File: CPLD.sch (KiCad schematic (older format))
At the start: 44 parts, among them J5 JTAG, J6 PMOD, Q1 IRLML6402, Q2 IRLML6402, SW2 SW_DIP_x06, U3 EPM7064STC100, X1 CFPS-72 50mhz

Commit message: started routing
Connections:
- wire segments 238 -> 236
- no-connect marks 8 -> 9
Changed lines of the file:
@@
 JTAG
-$Comp
-L THS-80:Altera-JTAG-10 J?
-U 1 1 5DC12FA5
-P 1000 1950
-AR Path="/5D0F9837/5DC12FA5" Ref="J?"  Part="1"
-AR Path="/5CFABACD/5D0BF766/5DC12FA5" Ref="J?"  Part="1"
-AR Path="/5D1AF052/5DC12FA5" Ref="J?"  Part="1"
-AR Path="/5DC12FA5" Ref="J?"  Part="1"
-AR Path="/5D70CA34/5DC12FA5" Ref="J5"  Part="1"
-F 0 "J5" H 1040 1950 50  0000 R CNN
-F 1 "JTAG" H 760 2450 50  0000 R CNN
-F 2 "Connector_PinHeader_2.54mm:PinHeader_2x05_P2.54mm_Vertical" V 850 2100 50  0001 C CNN
-F 3 "~" H -275 1400 50  0001 C CNN
-	1    1000 1950
-	1    0    0    -1
-$EndComp
 $Comp
 L power:VCC #PWR?
@@
 Wire Wire Line
 	900  1300 1200 1300
-Wire Wire Line
-	1500 1300 1500 1650
-Connection ~ 1200 1300
-Wire Wire Line
-	1200 1300 1500 1300
 Wire Wire Line
 	1500 1850 1700 1850
@@
 Text HLabel 7350 2075 2    50   Input ~ 0
 A[0..7]
-Text HLabel 3750 2400 0    50   Output ~ 0
-A[16..18]
 Text HLabel 7350 3150 2    50   Input ~ 0
 D[0..7]
@@
 L Device:R_Pack08 RN2
 U 1 1 5D75CC44
-P 10300 3300
-F 0 "RN2" V 9683 3300 50  0000 C CNN
-F 1 "680R" V 9774 3300 50  0000 C CNN
-F 2 "Resistor_SMD:R_Cat16-8" V 10775 3300 50  0001 C CNN
-F 3 "~" H 10300 3300 50  0001 C CNN
-	1    10300 3300
-	0    1    -1   0
-$EndComp
-Wire Wire Line
-	10500 3700 10500 3600
+P 10300 3400
+F 0 "RN2" V 9683 3400 50  0000 C CNN
+F 1 "680R" V 9774 3400 50  0000 C CNN
+F 2 "Resistor_SMD:R_Cat16-8" V 10775 3400 50  0001 C CNN
+F 3 "~" H 10300 3400 50  0001 C CNN
+	1    10300 3400
+	0    1    1    0
+$EndComp
+Wire Wire Line
+	10500 3000 10500 3100
+Connection ~ 10500 3100
+Wire Wire Line
+	10500 3100 10500 3200
+Connection ~ 10500 3200
+Wire Wire Line
+	10500 3200 10500 3300
+Connection ~ 10500 3300
+Wire Wire Line
+	10500 3300 10500 3350
+Connection ~ 10500 3400
+Wire Wire Line
+	10500 3400 10500 3500
+Connection ~ 10500 3500
+Wire Wire Line
+	10500 3500 10500 3600
 Connection ~ 10500 3600
 Wire Wire Line
-	10500 3600 10500 3500
-Connection ~ 10500 3500
-Wire Wire Line
-	10500 3500 10500 3400
-Connection ~ 10500 3400
-Wire Wire Line
-	10500 3400 10500 3350
-Connection ~ 10500 3300
-Wire Wire Line
-	10500 3300 10500 3200
-Connection ~ 10500 3200
-Wire Wire Line
-	10500 3200 10500 3100
-Connection ~ 10500 3100
-Wire Wire Line
-	10500 3100 10500 3000
+	10500 3600 10500 3700
 Wire Wire Line
 	10500 3350 10600 3350
 Connection ~ 10500 3350
 Wire Wire Line
-	10500 3350 10500 3300
+	10500 3350 10500 3400
 $Comp
 L power:VCC #PWR043
@@
 F 3 "" H 10600 3350 50  0001 C CNN
 	1    10600 3350
-	1    0    0    1
+	1    0    0    -1
 $EndComp
 $Comp
@@
 L Power_Protection:SP0504BAHT D12
 U 1 1 5DDF5EA5
-P 8900 6050
-F 0 "D12" H 9205 6096 50  0000 L CNN
-F 1 "SP0504BAHT" H 9205 6005 50  0000 L CNN
-F 2 "Package_TO_SOT_SMD:SOT-23-5" H 9200 6000 50  0001 L CNN
-F 3 "http://www.littelfuse.com/~/media/files/littelfuse/technical%20resources/documents/data%20sheets/sp05xxba.pdf" H 9025 6175 50  0001 C CNN
-	1    8900 6050
-	1    0    0    -1
+P 9000 6050
+F 0 "D12" H 8550 6050 50  0000 L CNN
+F 1 "SP0504BAHT" H 8350 5950 50  0000 L CNN
+F 2 "Package_TO_SOT_SMD:SOT-23-5" H 9300 6000 50  0001 L CNN
+F 3 "http://www.littelfuse.com/~/media/files/littelfuse/technical%20resources/documents/data%20sheets/sp05xxba.pdf" H 9125 6175 50  0001 C CNN
+	1    9000 6050
+	-1   0    0    -1
 $EndComp
 Wire Wire Line
@@
 L power:GND #PWR040
 U 1 1 5E09A200
-P 8900 6250
-F 0 "#PWR040" H 8900 6000 50  0001 C CNN
-F 1 "GND" H 8905 6077 50  0000 C CNN
-F 2 "" H 8900 6250 50  0001 C CNN
-F 3 "" H 8900 6250 50  0001 C CNN
-	1    8900 6250
-	1    0    0    -1
+P 9000 6250
+F 0 "#PWR040" H 9000 6000 50  0001 C CNN
+F 1 "GND" H 9005 6077 50  0000 C CNN
+F 2 "" H 9000 6250 50  0001 C CNN
+F 3 "" H 9000 6250 50  0001 C CNN
+	1    9000 6250
+	-1   0    0    -1
 $EndComp
 $Comp
@@
 Wire Wire Line
 	6650 1350 7250 1350
-Wire Wire Line
-	4450 2250 3850 2250
-Wire Wire Line
-	4450 2350 3850 2350
-Wire Wire Line
-	4450 2450 3850 2450
 Wire Wire Line
 	6650 1850 7250 1850
@@
 Text Label 6950 3450 0    50   ~ 0
 D7
-Text Label 4150 2250 2    50   ~ 0
-A18
-Text Label 4150 2350 2    50   ~ 0
-A17
-Text Label 4150 2450 2    50   ~ 0
-A16
-Entry Wire Line
-	3850 2250 3750 2350
-Entry Wire Line
-	3850 2350 3750 2450
-Entry Wire Line
-	3850 2450 3750 2550
 Entry Wire Line
 	7250 1850 7350 1950
@@
 $EndComp
 NoConn ~ 6650 1550
-NoConn ~ 4450 1950
-NoConn ~ 4450 2050
-NoConn ~ 4450 2150
+NoConn ~ 4450 2250
+NoConn ~ 4450 2350
+NoConn ~ 4450 2450
 $Comp
 L Device:C_Small C6
@@
 Wire Wire Line
 	6650 1450 7250 1450
+$Comp
+L THS-80:Altera-JTAG-10 J?
+U 1 1 5DC12FA5
+P 1000 1950
+AR Path="/5D0F9837/5DC12FA5" Ref="J?"  Part="1"
+AR Path="/5CFABACD/5D0BF766/5DC12FA5" Ref="J?"  Part="1"
+AR Path="/5D1AF052/5DC12FA5" Ref="J?"  Part="1"
+AR Path="/5DC12FA5" Ref="J?"  Part="1"
+AR Path="/5D70CA34/5DC12FA5" Ref="J5"  Part="1"
+F 0 "J5" H 1040 1950 50  0000 R CNN
+F 1 "JTAG" H 760 2450 50  0000 R CNN
+F 2 "Connector_PinHeader_2.54mm:PinHeader_2x05_P2.54mm_Vertical" V 850 2100 50  0001 C CNN
+F 3 "~" H -275 1400 50  0001 C CNN
+	1    1000 1950
+	1    0    0    -1
+$EndComp
+NoConn ~ 1500 1650
+Entry Wire Line
+	3850 2150 3750 2250
+Entry Wire Line
+	3850 2050 3750 2150
+Entry Wire Line
+	3850 1950 3750 2050
+Text Label 4150 2150 2    50   ~ 0
+A16
+Text Label 4150 2050 2    50   ~ 0
+A17
+Text Label 4150 1950 2    50   ~ 0
+A18
+Wire Wire Line
+	4450 2150 3850 2150
+Wire Wire Line
+	4450 2050 3850 2050
+Wire Wire Line
+	4450 1950 3850 1950
+Text HLabel 3750 2100 0    50   Output ~ 0
+A[16..18]
 Wire Bus Line
-	3750 2250 3750 2550
+	3750 1950 3750 2250
 Wire Bus Line
 	7350 1950 7350 2750

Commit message: more routing
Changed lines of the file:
@@
 Text HLabel 7350 3150 2    50   Input ~ 0
 D[0..7]
+Text Label 8925 3700 0    50   ~ 0
+LED0
+Text Label 8925 3600 0    50   ~ 0
+LED1
+Text Label 8925 3500 0    50   ~ 0
+LED2
+Text Label 8925 3400 0    50   ~ 0
+LED3
+Text Label 8925 3300 0    50   ~ 0
+LED4
+Text Label 8925 3200 0    50   ~ 0
+LED5
+Text Label 8925 3100 0    50   ~ 0
+LED6
 Text Label 8925 3000 0    50   ~ 0
-LED0
-Text Label 8925 3100 0    50   ~ 0
-LED1
-Text Label 8925 3200 0    50   ~ 0
-LED2
-Text Label 8925 3300 0    50   ~ 0
-LED3
-Text Label 8925 3400 0    50   ~ 0
-LED4
-Text Label 8925 3500 0    50   ~ 0
-LED5
-Text Label 8925 3600 0    50   ~ 0
-LED6
-Text Label 8925 3700 0    50   ~ 0
 LED7
+Wire Wire Line
+	8850 3100 9650 3100
+Wire Wire Line
+	8850 3200 9650 3200
+Wire Wire Line
+	8850 3300 9650 3300
+Wire Wire Line
+	8850 3400 9650 3400
+Wire Wire Line
+	8850 3500 9650 3500
 Wire Wire Line
 	8850 3600 9650 3600
 Wire Wire Line
-	8850 3500 9650 3500
-Wire Wire Line
-	8850 3400 9650 3400
-Wire Wire Line
-	8850 3300 9650 3300
-Wire Wire Line
-	8850 3200 9650 3200
-Wire Wire Line
-	8850 3100 9650 3100
+	8850 3700 9650 3700
 Wire Wire Line
 	8850 3000 9650 3000
-Wire Wire Line
-	8850 3700 9650 3700
 Text HLabel 3850 4350 0    50   Input ~ 0
 ~RESET

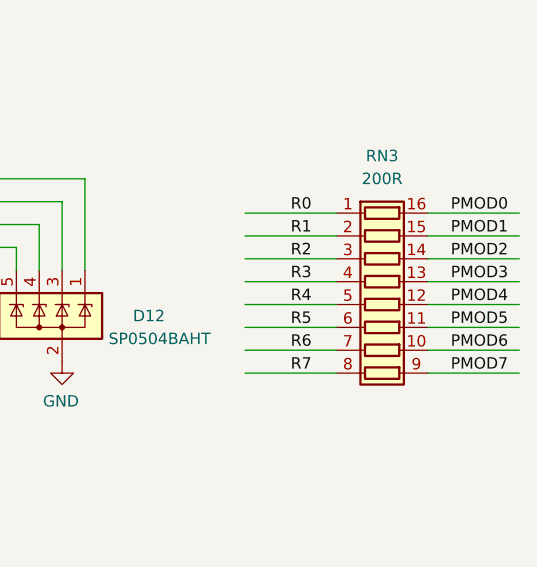
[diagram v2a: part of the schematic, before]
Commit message: finished routing, passed DRC
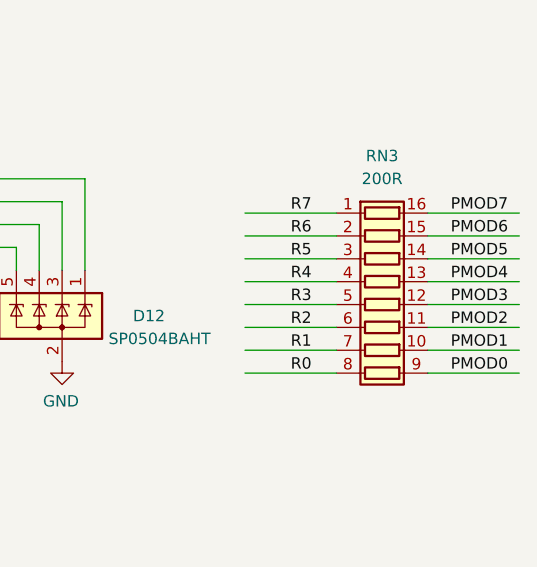
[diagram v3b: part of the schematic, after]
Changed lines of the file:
@@
 NoConn ~ 2400 5750
 Wire Wire Line
-	10200 5600 9800 5600
+	10200 6300 9800 6300
+Wire Wire Line
+	10200 6200 9800 6200
+Wire Wire Line
+	10200 6100 9800 6100
+Wire Wire Line
+	10200 6000 9800 6000
+Wire Wire Line
+	10200 5900 9800 5900
+Wire Wire Line
+	10200 5800 9800 5800
 Wire Wire Line
 	10200 5700 9800 5700
 Wire Wire Line
-	10200 5800 9800 5800
-Wire Wire Line
-	10200 5900 9800 5900
-Wire Wire Line
-	10200 6000 9800 6000
-Wire Wire Line
-	10200 6100 9800 6100
-Wire Wire Line
-	10200 6200 9800 6200
-Wire Wire Line
-	10200 6300 9800 6300
+	10200 5600 9800 5600
+Text Label 10000 6300 0    50   ~ 0
+R0
+Text Label 10000 6200 0    50   ~ 0
+R1
+Text Label 10000 6100 0    50   ~ 0
+R2
+Text Label 10000 6000 0    50   ~ 0
+R3
+Text Label 10000 5900 0    50   ~ 0
+R4
+Text Label 10000 5800 0    50   ~ 0
+R5
+Text Label 10000 5700 0    50   ~ 0
+R6
 Text Label 10000 5600 0    50   ~ 0
-R0
-Text Label 10000 5700 0    50   ~ 0
-R1
-Text Label 10000 5800 0    50   ~ 0
-R2
-Text Label 10000 5900 0    50   ~ 0
-R3
-Text Label 10000 6000 0    50   ~ 0
-R4
-Text Label 10000 6100 0    50   ~ 0
-R5
-Text Label 10000 6200 0    50   ~ 0
-R6
-Text Label 10000 6300 0    50   ~ 0
 R7
 $Comp
@@
 $EndComp
 Wire Wire Line
-	10600 5600 11000 5600
+	10600 6300 11000 6300
+Wire Wire Line
+	10600 6200 11000 6200
+Wire Wire Line
+	10600 6100 11000 6100
+Wire Wire Line
+	10600 6000 11000 6000
+Wire Wire Line
+	10600 5900 11000 5900
+Wire Wire Line
+	10600 5800 11000 5800
 Wire Wire Line
 	10600 5700 11000 5700
 Wire Wire Line
-	10600 5800 11000 5800
-Wire Wire Line
-	10600 5900 11000 5900
-Wire Wire Line
-	10600 6000 11000 6000
-Wire Wire Line
-	10600 6100 11000 6100
-Wire Wire Line
-	10600 6200 11000 6200
-Wire Wire Line
-	10600 6300 11000 6300
+	10600 5600 11000 5600
+Text Label 10700 6300 0    50   ~ 0
+PMOD0
+Text Label 10700 6200 0    50   ~ 0
+PMOD1
+Text Label 10700 6100 0    50   ~ 0
+PMOD2
+Text Label 10700 6000 0    50   ~ 0
+PMOD3
+Text Label 10700 5900 0    50   ~ 0
+PMOD4
+Text Label 10700 5800 0    50   ~ 0
+PMOD5
+Text Label 10700 5700 0    50   ~ 0
+PMOD6
 Text Label 10700 5600 0    50   ~ 0
-PMOD0
-Text Label 10700 5700 0    50   ~ 0
-PMOD1
-Text Label 10700 5800 0    50   ~ 0
-PMOD2
-Text Label 10700 5900 0    50   ~ 0
-PMOD3
-Text Label 10700 6000 0    50   ~ 0
-PMOD4
-Text Label 10700 6100 0    50   ~ 0
-PMOD5
-Text Label 10700 6200 0    50   ~ 0
-PMOD6
-Text Label 10700 6300 0    50   ~ 0
 PMOD7
 $Comp

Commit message: pmod changes
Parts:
- removed C14, C15: 100nF, Capacitor_SMD:C_0603_1608Metric_Pad1.05x0.95mm_HandSolder, symbol Device:C_Small
- removed D12, D3: SP0504BAHT, Package_TO_SOT_SMD:SOT-23-5, symbol Power_Protection:SP0504BAHT
- removed J6: PMOD, Connector_PinSocket_2.54mm:PinSocket_2x06_P2.54mm_Horizontal, symbol Connector_Generic:Conn_02x06_Top_Bottom
- removed RN3: 200R, Resistor_SMD:R_Cat16-8, symbol Device:R_Pack08
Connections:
- net labels added: OE1, OE2, PMOD[0..7]
- net labels removed: R0, R1, R2, R3, R4, R5, R6, R7
- wire segments 236 -> 198
- no-connect marks 9 -> 7
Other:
- moved on the sheet: C10, C11, C12, C13, C5, C6, C7, C8, C9, D10, D11, D13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

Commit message: finished routing, drc passed
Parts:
- removed D13: Green, LED_SMD:LED_0603_1608Metric_Pad1.05x0.95mm_HandSolder, symbol THS-80-rescue:LED-Device-max_breakout-rescue-sbc_z80-rescue
- removed Q1, Q2: IRLML6402, Package_TO_SOT_SMD:SOT-23, symbol THS-80:IRLML6402
- removed R14, R19: 100R, Resistor_SMD:R_0603_1608Metric_Pad1.05x0.95mm_HandSolder, symbol Device:R_Small
- removed R20: 360R, Resistor_SMD:R_0603_1608Metric_Pad1.05x0.95mm_HandSolder, symbol Device:R_Small
- added U12: 74HCT3G04, Package_SO:TSSOP-8_3x3mm_P0.65mm, symbol 74xGxx:74HCT3G04
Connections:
- net labels removed: OE2
- wire segments 198 -> 183
- no-connect marks 7 -> 8
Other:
- note removed: "JTAG"
- note removed: "ROM Paged"
- moved on the sheet: C10, C11, C12, C13, C5, C6, C7, C8, C9, D10, D11, D2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

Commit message: track cleanup, fixed slots in ground plane
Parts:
- U12: symbol 74xGxx:74HCT3G04 -> THS-80-rescue:74HCT3G04-74xGxx
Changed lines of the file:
@@
 	6150 4450 6750 4450
 $Comp
-L 74xGxx:74HCT3G04 U?
+L THS-80-rescue:74HCT3G04-74xGxx U?
 U 3 1 5D9FA47F
 P 5400 5500
 AR Path="/5D6224DC/5D9FA47F" Ref="U?"  Part="3"
 AR Path="/5D70CA34/5D9FA47F" Ref="U12"  Part="3"
+AR Path="/5D9FA47F" Ref="U12"  Part="3"
 F 0 "U12" H 5375 5767 50  0000 C CNN
 F 1 "74HCT3G04" H 5375 5676 50  0000 C CNN

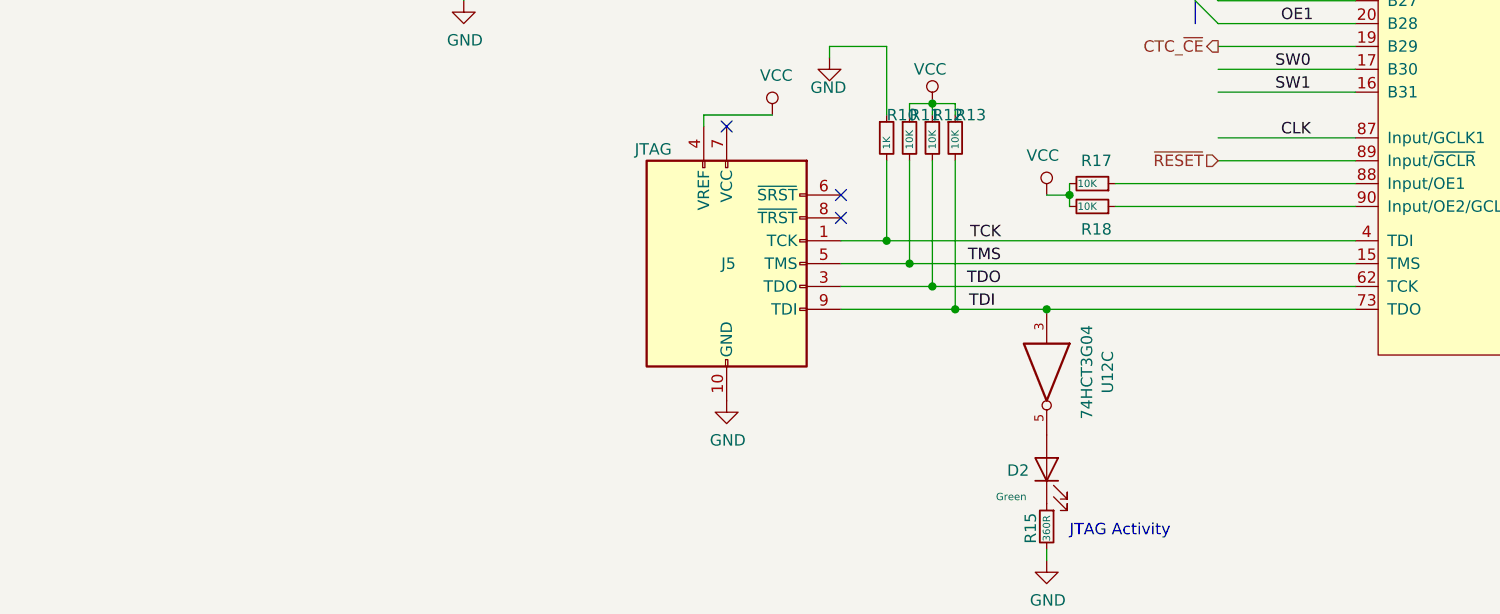
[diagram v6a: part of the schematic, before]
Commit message: fixed gnd plane breaks, adjust silk screens
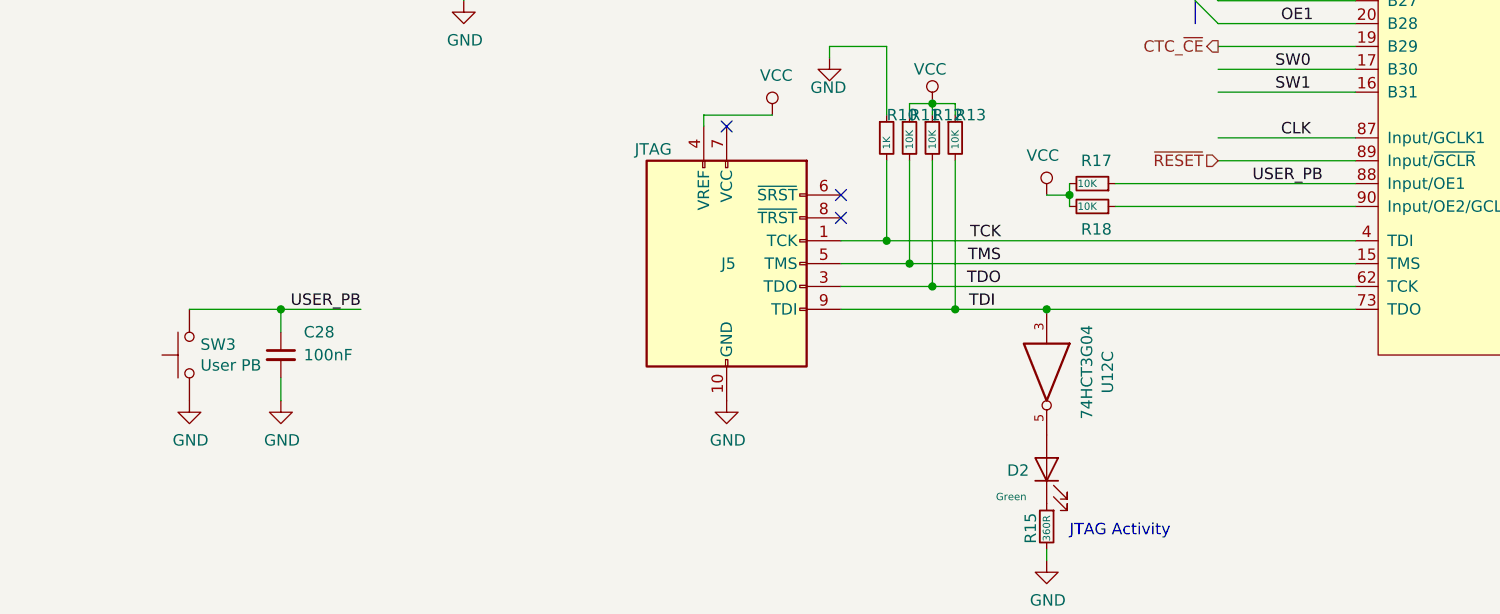
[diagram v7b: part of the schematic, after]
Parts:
- added C28: 100nF, Capacitor_SMD:C_0603_1608Metric_Pad1.05x0.95mm_HandSolder, symbol Device:C_Small
- added SW3: User PB, Button_Switch_SMD:SW_SPST_FSMSM, symbol Switch:SW_Push
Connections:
- net labels added: USER_PB
- wire segments 183 -> 187
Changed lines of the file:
@@
 Wire Wire Line
 	3100 1950 3525 1950
+Text Label 6300 4650 0    50   ~ 0
+USER_PB
+$Comp
+L Switch:SW_Push SW3
+U 1 1 5D8710D3
+P 1650 5400
+F 0 "SW3" V 1696 5352 50  0000 R CNN
+F 1 "User PB" V 1605 5352 50  0000 R CNN
+F 2 "Button_Switch_SMD:SW_SPST_FSMSM" H 1650 5600 50  0001 C CNN
+F 3 "~" H 1650 5600 50  0001 C CNN
+	1    1650 5400
+	0    -1   -1   0
+$EndComp
+$Comp
+L power:GND #PWR082
+U 1 1 5D8738FA
+P 1650 5600
+F 0 "#PWR082" H 1650 5350 50  0001 C CNN
+F 1 "GND" H 1655 5427 50  0000 C CNN
+F 2 "" H 1650 5600 50  0001 C CNN
+F 3 "" H 1650 5600 50  0001 C CNN
+	1    1650 5600
+	1    0    0    -1
+$EndComp
+Wire Wire Line
+	1650 5200 2050 5200
+$Comp
+L Device:C_Small C?
+U 1 1 5D88E389
+P 2050 5400
+AR Path="/5D65A6A0/5D88E389" Ref="C?"  Part="1"
+AR Path="/5D88E389" Ref="C?"  Part="1"
+AR Path="/5D70CA34/5D88E389" Ref="C28"  Part="1"
+F 0 "C28" H 2150 5500 50  0000 L CNN
+F 1 "100nF" H 2150 5400 50  0000 L CNN
+F 2 "Capacitor_SMD:C_0603_1608Metric_Pad1.05x0.95mm_HandSolder" H 2050 5400 50  0001 C CNN
+F 3 "https://www.mouser.com/datasheet/2/396/mlcc02_e-1307760.pdf" H 2050 5400 50  0001 C CNN
+F 4 "Multilayer Ceramic Capacitors MLCC - SMD/SMT 0603 10V 10nF 5% X7R" H 2142 5546 50  0001 C CNN "Description"
+F 5 "Taiyo Yuden" H 2050 5400 50  0001 C CNN "MFR"
+F 6 "JMK107B7474KA-T" H 2050 5400 50  0001 C CNN "MPN"
+F 7 "963-JMK107B7474KA-T" H 2142 5546 50  0001 C CNN "SPN"
+F 8 "Mouser" H 2050 5400 50  0001 C CNN "SPR"
+F 9 "https://www.mouser.com/ProductDetail/963-JMK107B7474KA-T" H 2142 5546 50  0001 C CNN "SPURL"
+	1    2050 5400
+	1    0    0    -1
+$EndComp
+Wire Wire Line
+	2050 5300 2050 5200
+$Comp
+L power:GND #PWR083
+U 1 1 5D8C3559
+P 2050 5600
+F 0 "#PWR083" H 2050 5350 50  0001 C CNN
+F 1 "GND" H 2055 5427 50  0000 C CNN
+F 2 "" H 2050 5600 50  0001 C CNN
+F 3 "" H 2050 5600 50  0001 C CNN
+	1    2050 5600
+	1    0    0    -1
+$EndComp
+Wire Wire Line
+	2050 5500 2050 5600
+Text Label 2400 5200 2    50   ~ 0
+USER_PB
+Connection ~ 2050 5200
+Wire Wire Line
+	2050 5200 2400 5200
 Wire Bus Line
 	6050 2450 6050 2750
